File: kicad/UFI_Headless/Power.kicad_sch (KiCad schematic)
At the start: 41 parts, among them J1 USB-C, J2 12V DC 5.5/2.1, J3 FDD_PWR, U1 USBLC6-2SC6, U2 TPS54202DDC, U3 TPS2116DRL, U4 AP7361C-33E

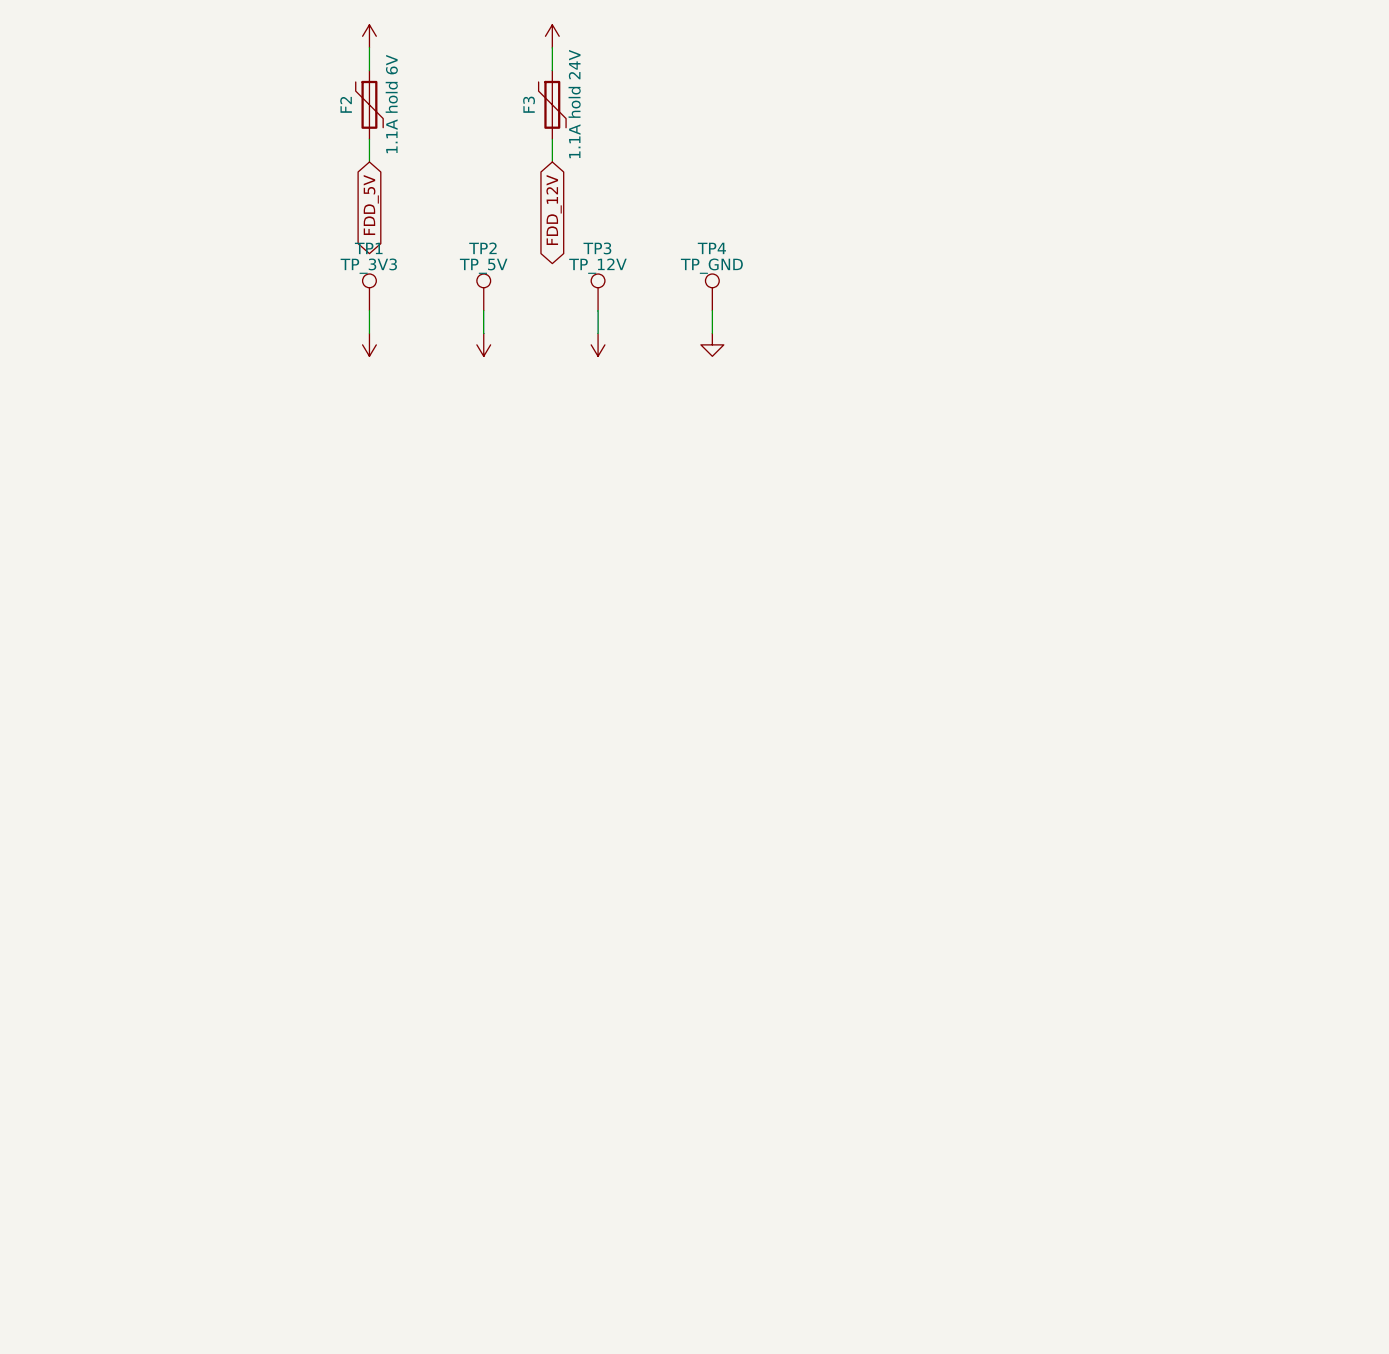
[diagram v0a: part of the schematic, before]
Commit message: UFI Headless v0.5: switched/measured drive supplies, write lock, microSD, expansion
Hardware (A1-A9): FDD_5V/FDD_12V high-side P-FET switches (off in reset)
with 0.1R + INA180A1 current sense, TVS at both outputs; WRITE LOCK
jumper J11 gates WGATE through 74LVC1G32 (TP8 now shows the gated
signal); expansion header J9 (I2C1, 2 GPIO, button lines, 3V3/5V),
buttons SW3/SW4; microSD J10 on SDMMC2 with the card slot facing the
top edge; board ID divider on PA4; test points TP7/TP8.  12V reverse
protection already existed; 8-inch 50-pin port left out (board size).
ECO placed 37 parts; Freerouting plus hand routes for the rest.
New scripts/eco/ tools (maze router, route check, cluster/occupancy
maps, via scan), add_silk_label.py no longer crashes on re-placement.
ERC 0, DRC 0 incl. warnings, 0 unconnected, parity clean, no via-in-pad;
fab outputs regenerated (146 CPL rows).
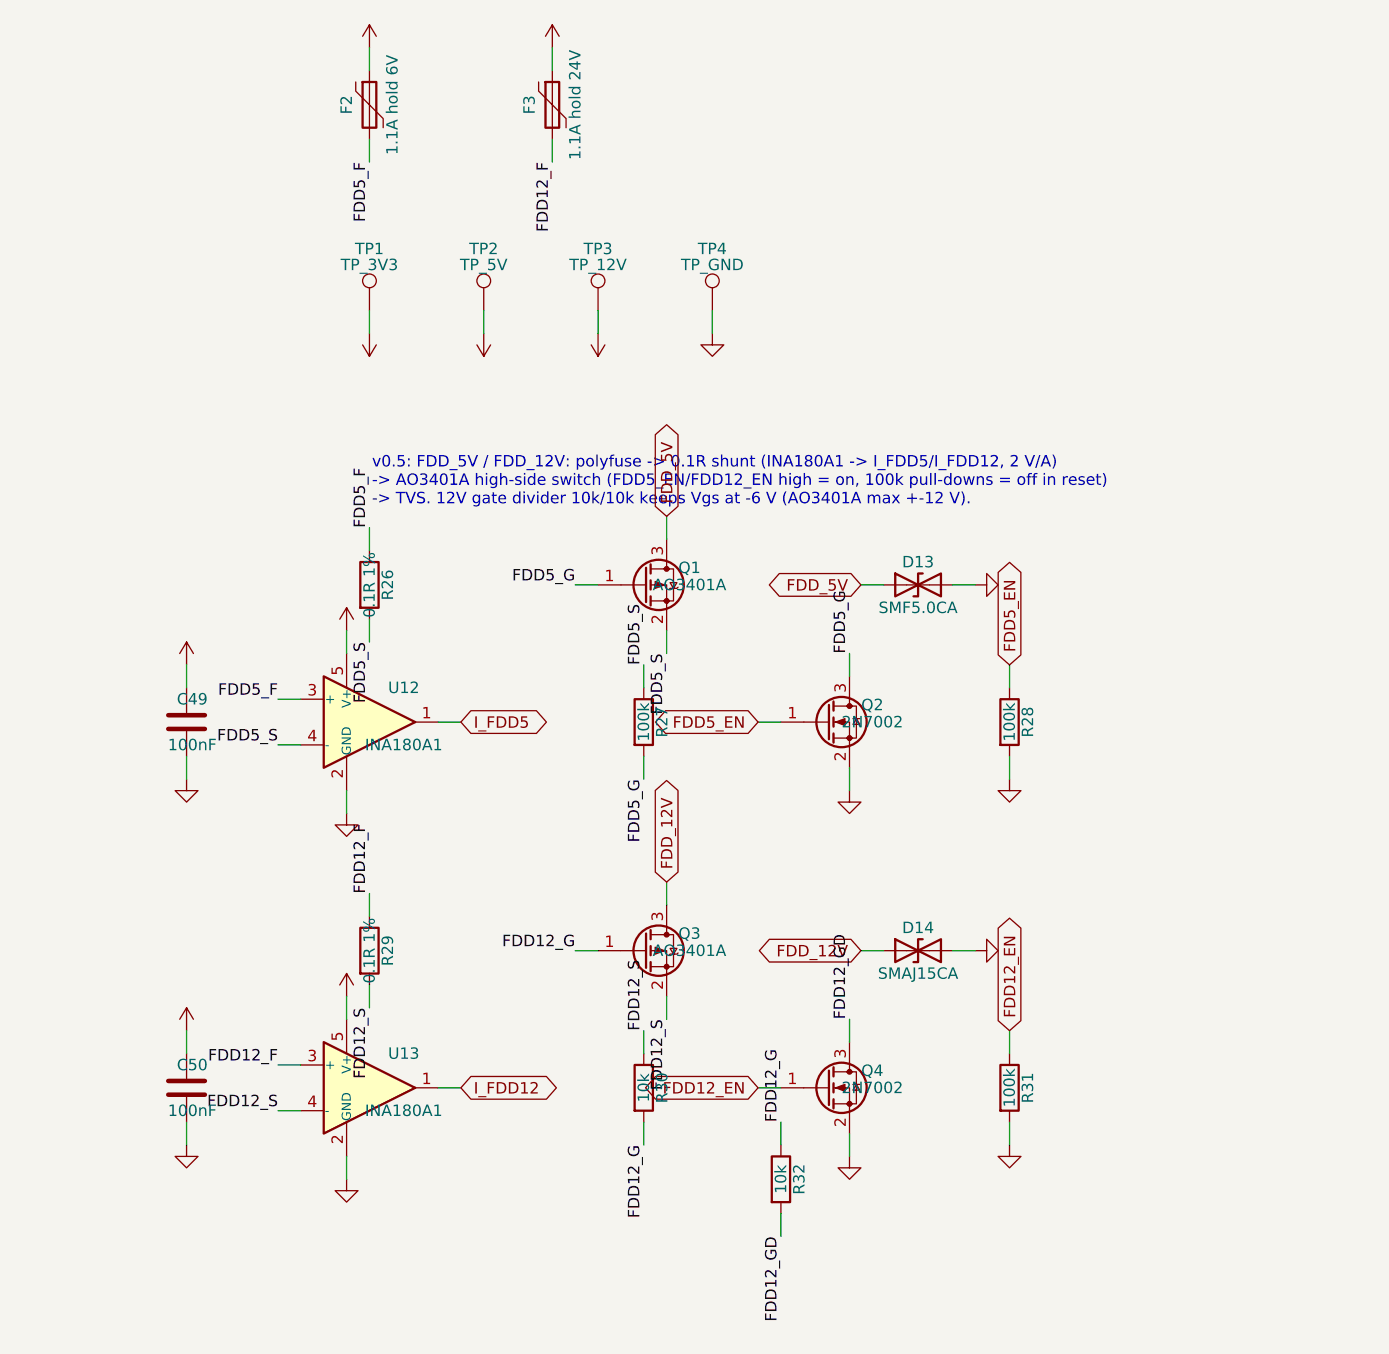
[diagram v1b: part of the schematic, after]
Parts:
- added C49, C50: 100nF, Capacitor_SMD:C_0603_1608Metric, symbol Device:C
- added D13: SMF5.0CA, Diode_SMD:D_SMF, symbol Device:D_TVS
- added D14: SMAJ15CA, Diode_SMD:D_SMA, symbol Device:D_TVS
- added Q1, Q3: AO3401A, Package_TO_SOT_SMD:SOT-23, symbol Transistor_FET:AO3401A
- added Q2, Q4: 2N7002, Package_TO_SOT_SMD:SOT-23, symbol Transistor_FET:2N7002
- added R26, R29: 0.1R 1%, Resistor_SMD:R_1206_3216Metric, symbol Device:R
- added R27, R28, R31: 100k, Resistor_SMD:R_0603_1608Metric, symbol Device:R
- added R30, R32: 10k, Resistor_SMD:R_0603_1608Metric, symbol Device:R
- added U12, U13: INA180A1, Package_TO_SOT_SMD:SOT-23-5, symbol Amplifier_Current:INA180A1
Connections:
- net +3V3: now also C49.1, C50.1, U12.5 (V+), U13.5 (V+)
- net FDD_12V: now also D14.1 (A1), Q3.3 (D); no longer F3.2
- net FDD_5V: now also D13.1 (A1), Q1.3 (D); no longer F2.2
- net GND: now also C49.2, C50.2, D13.2 (A2), D14.2 (A2), Q2.2 (S), Q4.2 (S), R28.2, R31.2, U12.2 (GND), U13.2 (GND)
- new net FDD12_EN: Q4.1 (G), R31.1
- new net FDD12_F: F3.2, R29.1, U13.3 (+)
- new net FDD12_G: Q3.1 (G), R30.2, R32.1
- new net FDD12_GD: Q4.3 (D), R32.2
- new net FDD12_S: Q3.2 (S), R29.2, R30.1, U13.4 (-)
- new net FDD5_EN: Q2.1 (G), R28.1
- new net FDD5_F: F2.2, R26.1, U12.3 (+)
- new net FDD5_G: Q1.1 (G), Q2.3 (D), R27.2
- new net FDD5_S: Q1.2 (S), R26.2, R27.1, U12.4 (-)
- new net I_FDD12: U13.1
- new net I_FDD5: U12.1
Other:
- note added: "v0.5: FDD_5V / FDD_12V: polyfuse -> 0.1R shunt (INA180A1 -> I_FDD5/I_FDD12, 2 V/A) -> AO3401A high-side switch (FDD5_EN/FDD12_EN high = on, 100k pull-downs = off in reset) -> TVS. 12V gate divider 10k/10k keeps Vgs at -6 V (AO3401A max +-12 V)."

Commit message: v0.7: internal USB 2.0 header J16, PC PSU input J17 (F4, D17), 5V source jumper J18, Disk II sync sensor input J19; DRC 0, parity 0, fab data
route_try.py: own-net THT holes are no obstacle.
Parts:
- added D17: SMF5.0CA, Diode_SMD:D_SMF, symbol Device:D_TVS
- added F4: 1.5A hold, Fuse:Fuse_1812_4532Metric, symbol Device:Polyfuse
- added J16: USB_HDR, Connector_PinHeader_2.54mm:PinHeader_2x05_P2.54mm_Vertical, symbol Connector_Generic:Conn_02x05_Odd_Even
- added J17: PSU_IN, Connector_PinHeader_2.54mm:PinHeader_1x04_P2.54mm_Vertical, symbol Connector_Generic:Conn_01x04
- added J18: 5V_SEL, Connector_PinHeader_2.54mm:PinHeader_1x03_P2.54mm_Vertical, symbol Connector_Generic:Conn_01x03
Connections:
- net +12V_IN: now also J17.4 (Pin_4)
- net +5V_DRV: now also J18.1 (Pin_1); no longer C8.1, C9.1, R5.1, U3.3 (VIN1), U3.5 (MODE)
- net GND: now also D17.2 (A2), J16.7 (Pin_7), J16.8 (Pin_8), J17.2 (Pin_2), J17.3 (Pin_3)
- net USB_DM: now also J16.3 (Pin_3)
- net USB_DP: now also J16.5 (Pin_5)
- net VBUS: now also J16.1 (Pin_1)
- new net +5V_PRI: C8.1, C9.1, J18.2 (Pin_2), R5.1, U3.3 (VIN1), U3.5 (MODE)
- new net +5V_PSU: F4.1, J17.1 (Pin_1)
- new net +5V_PSU_F: D17.1 (A1), F4.2, J18.3 (Pin_3)
- no-connect marks 3 -> 8
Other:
- note added: "v0.7: J16 internal USB header (1 +5V, 3 D-, 5 D+, 7/8 GND, pin 9 not fitted = key) parallel to USB-C: one host only. J17 PC PSU (Berg 1 +5V, 2/3 GND, 4 +12V -> +12V_IN): J2 or J17, not both. J18 5V priority source: 1-2 = 12V buck (default), 2-3 = PSU +5V; USB VBUS is the fallback."

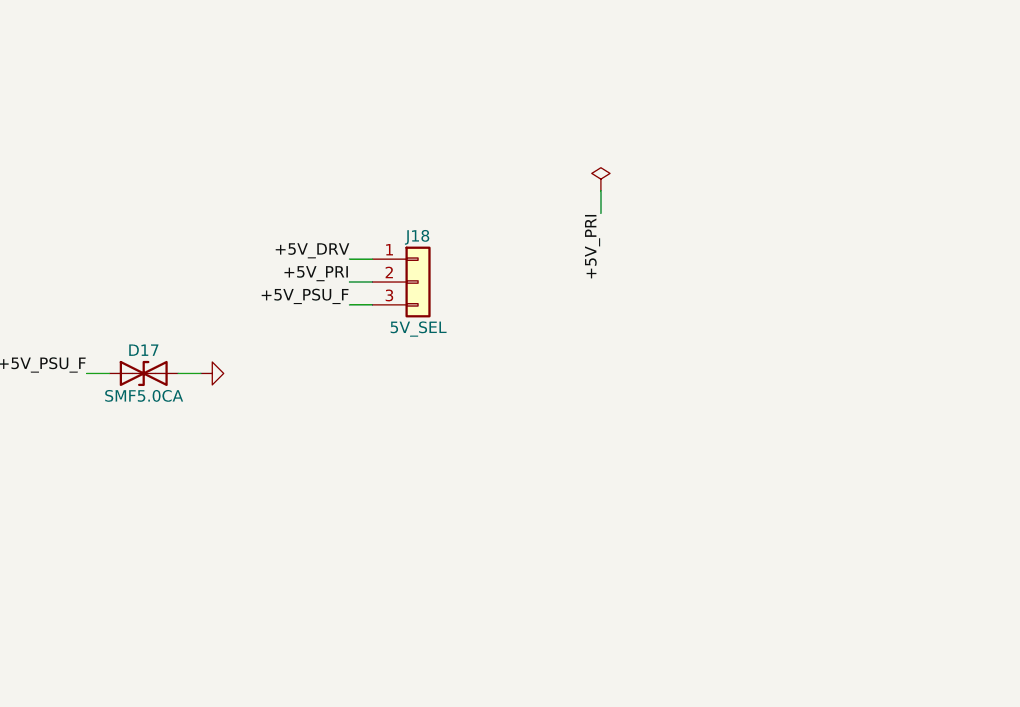
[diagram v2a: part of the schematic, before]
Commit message: KiCad v0.7 rework, schematic stages A1-A3: automatic 5 V source selection, discrete FDD termination, front-panel header - Power: J18 (5V_SEL jumper) removed, U19 TPS2116DRL selects external 5 V (J17, priority) or the 12 V buck automatically (R72 33k / R73 10k PR1 divider, C57 1 uF, status via R74 10k to +3V3 on test point TP9 TP_5V_SEL), PWR_FLAG moved to +5V_PSU_F; Flux_Interface / IEC_Bus / FDD_Connectors: RN1-RN8 (1k R_Pack04) replaced by 25 discrete 0603 1k resistors R75-R99 on the same nets (17 FDD lines, 5 IEC, 3 Amiga), array stubs, per-pin +5V symbols and orphan no-connects removed; MCU_Core: J9 EXPANSION and J13 MODE_SW removed, J12 becomes a keyed 2x8 IDC front-panel header FRONT (1 +3V3, 3 ACT, 5 ERR, 7 USB, 9 FDD, 11 PWR via R34-R37 and new R100 330 R, 13 BTN_A, 14 BTN_B, 15 MODE1, 16 MODE2 via R101-R104 470 R and TVS D18-D21, even pins 2-12 GND), on-board LEDs D5-D8 with R12-R15 removed (D4 ACT stays), SW3/SW4 marked DNP (buttons on the front); lib_symbols for Conn_02x08_Odd_Even and D_TVS added to MCU_Core; ERC over the whole project 0 errors / 0 warnings. Design brief docs/PCB_Revision_Empfehlungen_2026-10-24.md (decisions of 2026-10-24: power as before minus J18, input edge vs. drive edge, DB23 Amiga at the drive edge, W5500 LAN at the input edge, 32x 0603 termination), bring-up procedure docs/Bringup_2026-10-24.md (USB-C J1 soldered rotated 180 deg on the first board). Open for A4/A5: INDEX_SIM needs its own timer-capable MCU pin (PE1 is now the MODE2 line; firmware pin map changes in the same commit as the schematic), I2C SCL/SDA get 4 test pads, D18-D21 to be swapped for low-leakage ESD diodes (SMF3.3CA leaks up to 1 mA at 3.3 V against ~40k internal pull-ups) plus ESD on the five LED lines, +3V3 on J12 pin 1 to be fed through a 1k series resistor, loopback block, LA header, J11 slide switch, DIN-6 and DB23, W5500, then layout (USB-C edge cutout, input/output edges). Layout (.kicad_pcb) not yet touched.
Claude-Session: https://claude.ai/code/sessi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
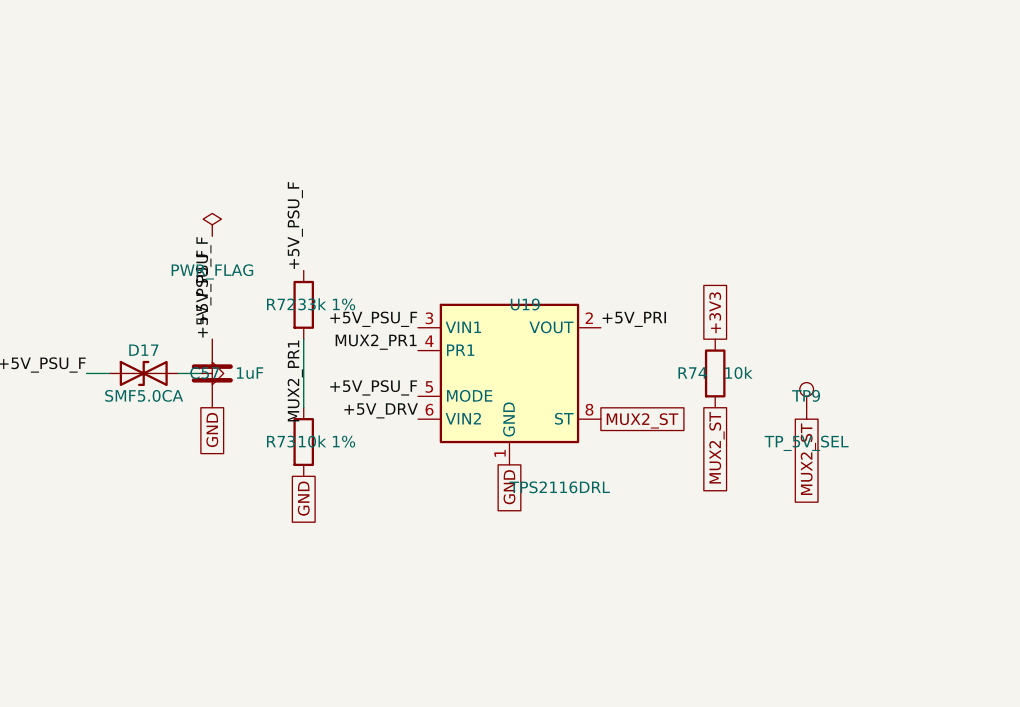
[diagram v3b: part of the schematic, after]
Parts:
- removed J18: 5V_SEL, Connector_PinHeader_2.54mm:PinHeader_1x03_P2.54mm_Vertical, symbol Connector_Generic:Conn_01x03
- added C57: 1uF, Capacitor_SMD:C_0603_1608Metric, symbol Device:C
- added R72: 33k 1%, Resistor_SMD:R_0603_1608Metric, symbol Device:R
- added R73: 10k 1%, Resistor_SMD:R_0603_1608Metric, symbol Device:R
- added R74: 10k, Resistor_SMD:R_0603_1608Metric, symbol Device:R
- added TP9: TP_5V_SEL, TestPoint:TestPoint_Pad_D1.5mm, symbol Connector:TestPoint
- added U19: TPS2116DRL, Package_TO_SOT_SMD:SOT-583-8, symbol Power_Management:TPS2116DRL
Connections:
- net +3V3: now also R74.1
- net +5V_DRV: now also U19.6 (VIN2)
- net +5V_PRI: now also U19.2 (VOUT), U19.7 (VOUT)
- net +5V_PSU_F: now also C57.1, R72.1, U19.3 (VIN1), U19.5 (MODE)
- net GND: now also C57.2, R73.2, U19.1 (GND)
- new net MUX2_PR1: R72.2, R73.1, U19.4 (PR1)
- new net MUX2_ST: R74.2, TP9.1, U19.8 (ST)

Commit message: KiCad v0.7 rework, stage B2: board v1.0 placed and routed, DRC 0 errors / 0 warnings / 0 unconnected with schematic parity - J1 USB-C and J22 RJ45 turned so that their openings cross the input edge (rot 180 at y 2.66 / 13.11 mm; at rotation 0 both library footprints open towards the board, which is how the USB-C receptacle stood since v0.1), DRU rule idc_edge_silk extended to J1/J22/J12 (silk over the edge is clipped by the fab, justified in the file), old J9 spoke rule removed; final placement by scripts/eco/place_v10.py plus relayout_lan.py (Y2/C59/C60/R109 crystal cluster and the 3V3A filter re-laid under U23, SW3 DNP parked on B.Cu under J22 pending the owner's SW3/SW4 decision); routing: the make_pcb.sh pipeline (Freerouting 2.4.1) hit the 1800 s timeout and left 154 connections open at the 0.5-mm QFP rows of U5/U23, so the rest was done with new ECO tools - rip_net.py (corridors), fanout.py (0.5/0.25 mm dogbone vias in two rows), shrink_vias.py, batch_route.py (A* over the kicad-cli DRC JSON: every grid step checked as a segment, string-pulling per layer run, via cost in mm, start at fan-out vias, ROUTE_CLR/ROUTE_W overrides), add_vias.py (GND stitches for isolated GND pads U23.29, C29.2, U13.2/C50.2), drop_pours.py + power_pours.py (stale supply pours had bridged five missing +5V tracks at R92-R96), trim_dangling.py, hide_small_refs.py (references only for ICs, connectors, switches, crystals, fuses, inductors, D4), place_silk.py (references/texts to the nearest free silk spot, F and B); schematic: TP9-TP13 and JP4 in_bom no (set_in_bom.py), footprint Description fields synced from the symbols (netlist.py/sync_fields.py) so the parity check is clean; picture docs/layout_v1.0_2026-10-24.png; PLAN.md B2 done, kicad README layout v1.0 section, scripts/eco/README.md. Owner skill pcb-routing (installed today) applied: routing_rules.json with the 16 load nets (F1/F4 1.5 A, F2/F3 1.1 A with cut-off above 1.5 A, buck 2 A) and 24 load paths, net class Load 1.0 mm / 0.8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
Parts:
- TP9: now left out of the parts list
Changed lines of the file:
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@@
 		(unit 1)
 		(exclude_from_sim no)
-		(in_bom yes)
+		(in_bom no)
 		(on_board yes)
 		(dnp no)
